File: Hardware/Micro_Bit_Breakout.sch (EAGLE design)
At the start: 9 parts, among them J1 M22LOCK, X1 EDGE-80PTH-RA

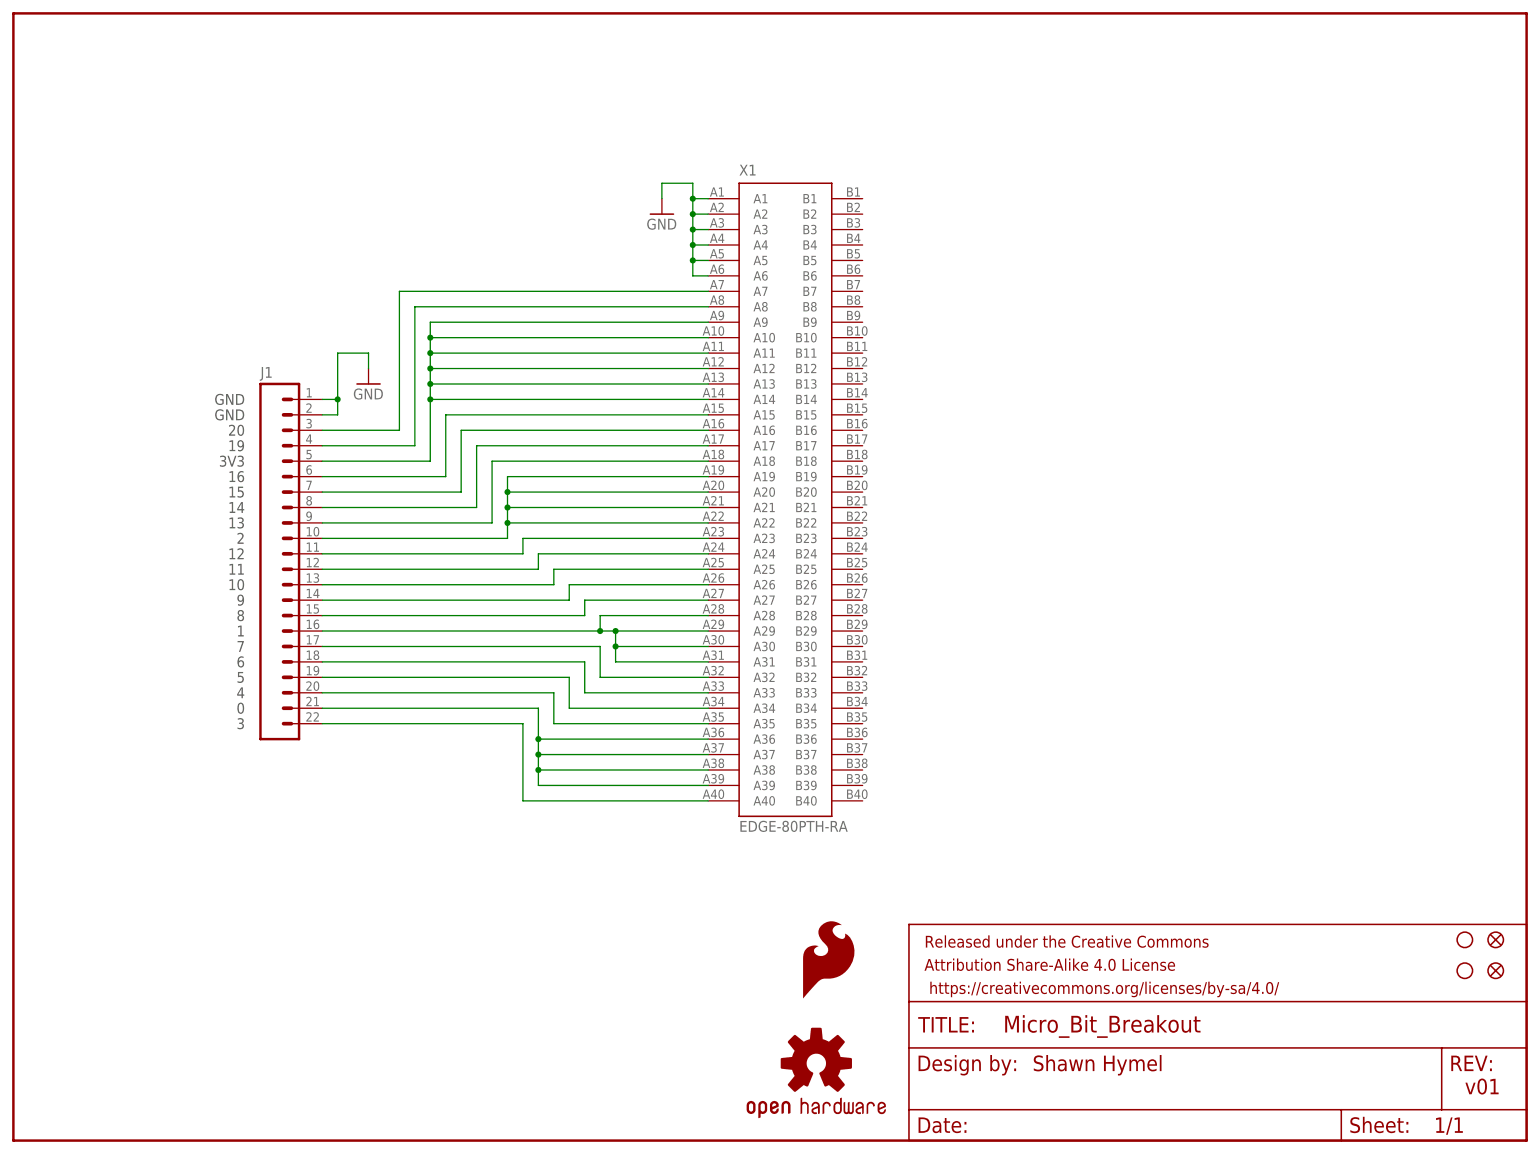
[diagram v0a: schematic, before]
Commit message: Moved brd outline down
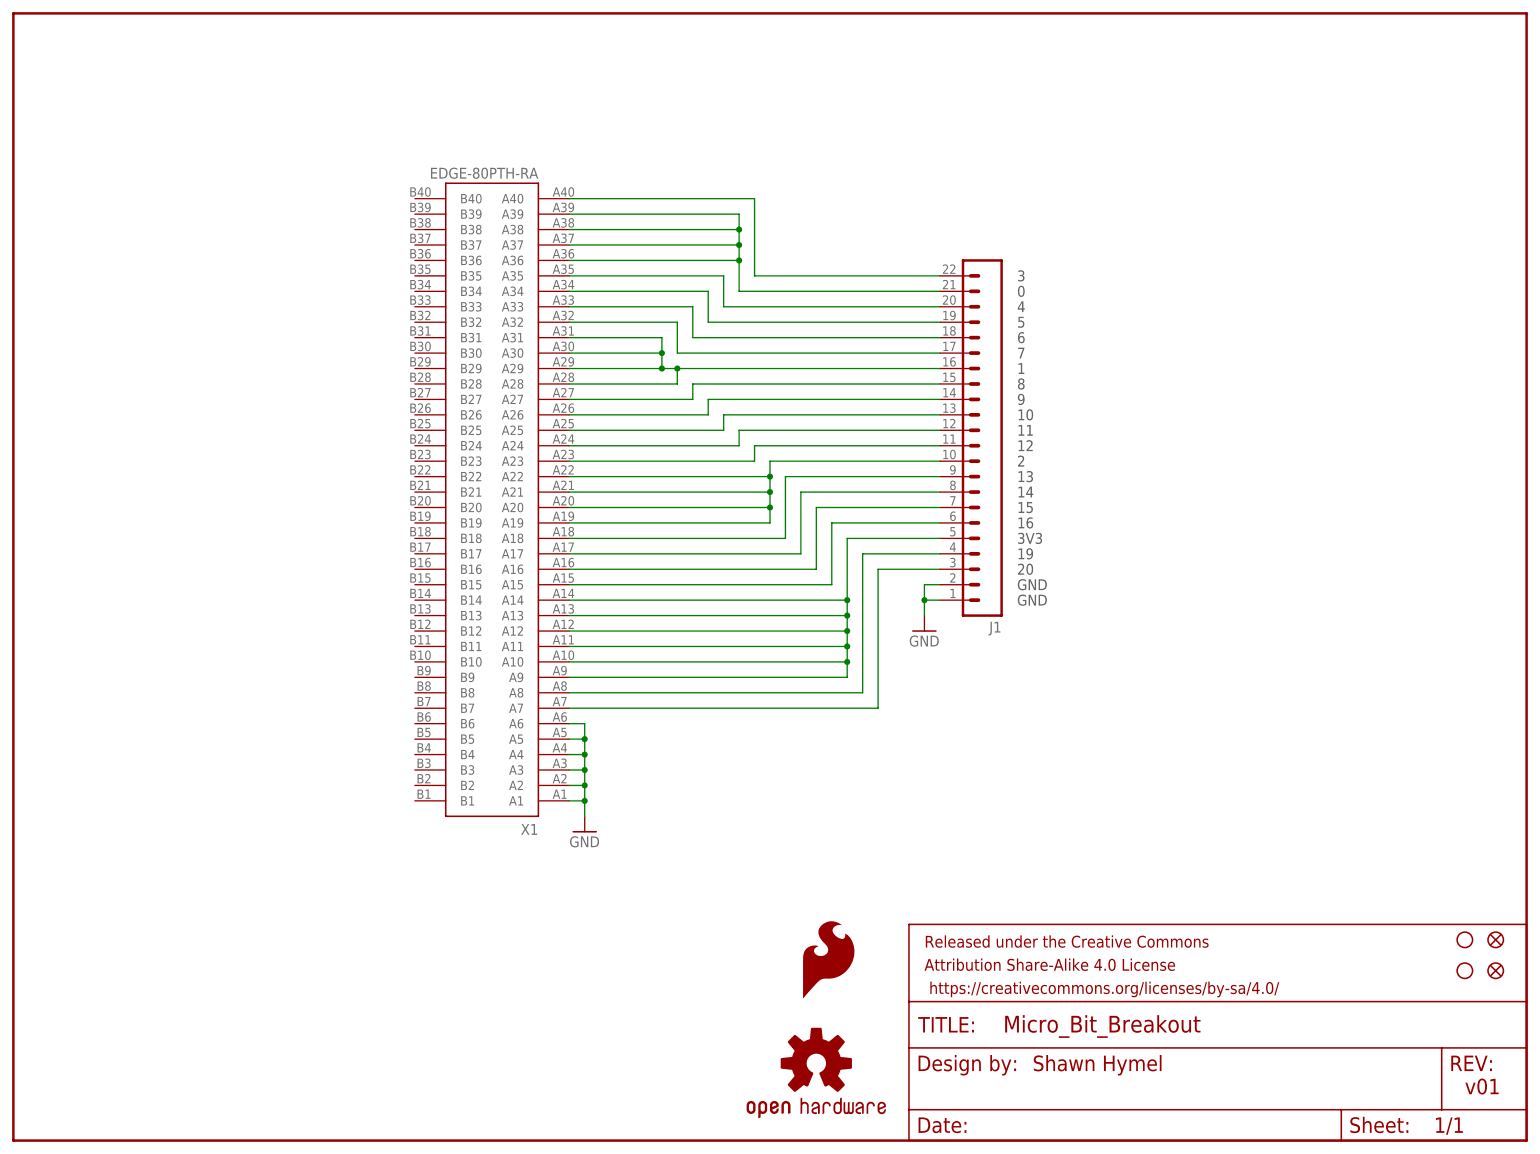
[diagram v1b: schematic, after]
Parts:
- J1: value M22LOCK -> M22PTH; device SparkFun-Connectors:M22LOCK -> local_lib:M22PTH
- X1: device SparkFun-Connectors:EDGE-80PTH-RA -> local_lib:EDGE-80PTH-RA
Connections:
- net N$10 renamed 12
- net N$11 renamed 11
- net N$12 renamed 10
- net N$13 renamed 9
- net N$14 renamed 8
- net N$15 renamed 1
- net N$17 renamed 7
- net N$18 renamed 6
- net N$19 renamed 5
- net N$2 renamed 16
- net N$20 renamed 4
- net N$21 renamed 0
- net N$22 renamed 3
- net N$3 renamed 20
- net N$4 renamed 19
- net N$5 renamed 3V3
- net N$6 renamed 15
- net N$7 renamed 14
- net N$8 renamed 13
- net N$9 renamed 2
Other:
- moved on the sheet: J1, X1

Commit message: Changed layout to have pin numbers in order. Added prettier silk.
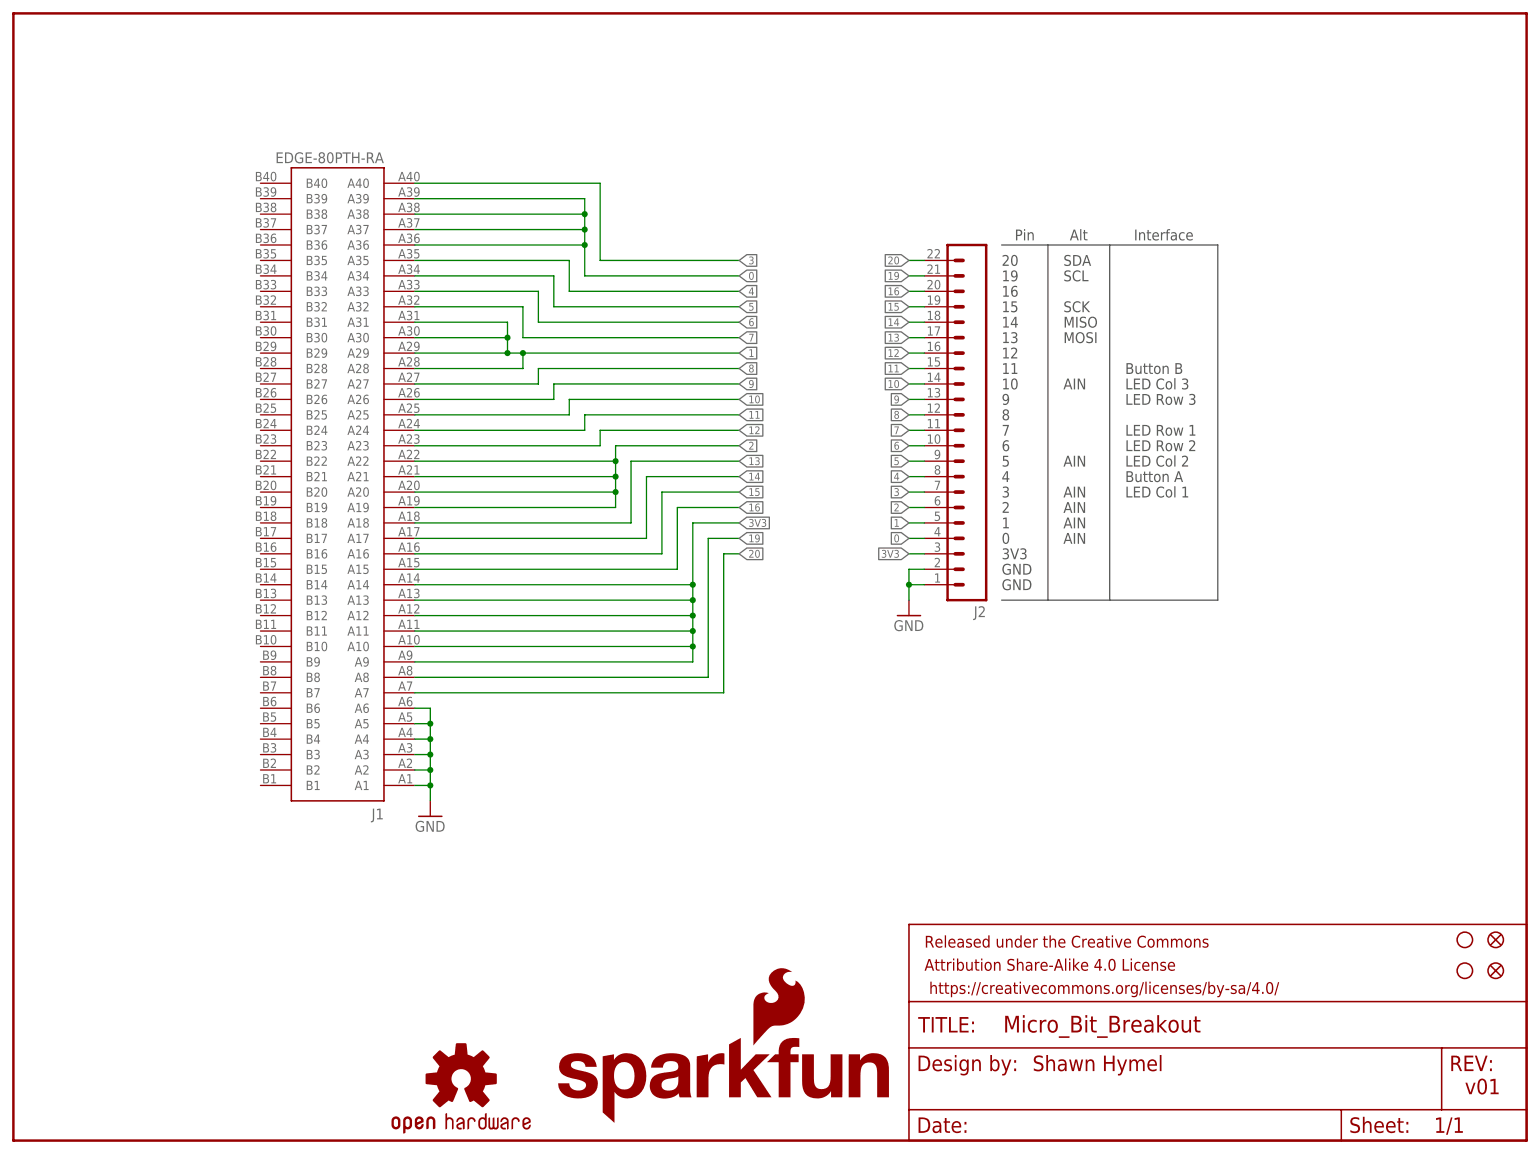
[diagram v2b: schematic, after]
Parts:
- removed LOGO1: SFE_LOGO_FLAME.1_INCH, SparkFun-Aesthetics:SFE_LOGO_FLAME.1_INCH
- removed X1: EDGE-80PTH-RA, local_lib:EDGE-80PTH-RA
- added J2: M22PTH, local_lib:M22PTH
- added LOGO2: SFE_LOGO_NAME_FLAME.1_INCH, SparkFun-Aesthetics:SFE_LOGO_NAME_FLAME.1_INCH
- J1: value M22PTH -> EDGE-80PTH-RA; device local_lib:M22PTH -> local_lib:EDGE-80PTH-RA
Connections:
- net 0: now also J1.A36, J1.A37, J1.A38, J1.A39, J2.4; no longer J1.21, X1.A36, X1.A37, X1.A38, X1.A39
- net 1: now also J1.A28, J1.A29, J1.A30, J1.A31, J2.5; no longer J1.16, X1.A28, X1.A29, X1.A30, X1.A31
- net 10: now also J1.A25, J2.14; no longer J1.13, X1.A25
- net 11: now also J1.A24, J2.15; no longer J1.12, X1.A24
- net 12: now also J1.A23, J2.16; no longer J1.11, X1.A23
- net 13: now also J1.A18, J2.17; no longer J1.9, X1.A18
- net 14: now also J1.A17, J2.18; no longer J1.8, X1.A17
- net 15: now also J1.A16, J2.19; no longer J1.7, X1.A16
- net 16: now also J1.A15, J2.20; no longer J1.6, X1.A15
- net 19: now also J1.A8, J2.21; no longer J1.4, X1.A8
- net 2: now also J1.A19, J1.A20, J1.A21, J1.A22, J2.6; no longer J1.10, X1.A19, X1.A20, X1.A21, X1.A22
- net 20: now also J1.A7, J2.22; no longer J1.3, X1.A7
- net 3: now also J1.A40, J2.7; no longer J1.22, X1.A40
- net 3V3: now also J1.A10, J1.A11, J1.A12, J1.A13, J1.A14, J1.A9, J2.3; no longer J1.5, X1.A10, X1.A11, X1.A12, X1.A13, X1.A14, X1.A9
- net 4: now also J1.A35, J2.8; no longer J1.20, X1.A35
- net 5: now also J1.A34, J2.9; no longer J1.19, X1.A34
- net 6: now also J1.A33, J2.10; no longer J1.18, X1.A33
- net 7: now also J1.A32, J2.11; no longer J1.17, X1.A32
- net 8: now also J1.A27, J2.12; no longer J1.15, X1.A27
- net 9: now also J1.A26, J2.13; no longer J1.14, X1.A26
- net GND: now also J1.A1, J1.A2, J1.A3, J1.A4, J1.A5, J1.A6, J2.1, J2.2; no longer J1.1, J1.2, X1.A1, X1.A2, X1.A3, X1.A4, X1.A5, X1.A6
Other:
- note added: "AIN"
- note added: "Alt"
- note added: "Button A"
- note added: "Button B"
- note added: "Interface"
- note added: "LED Col 1"
- note added: "LED Col 2"
- note added: "LED Col 3"
- note added: "LED Row 1"
- note added: "LED Row 2"
- note added: "LED Row 3"
- note added: "MISO"
- note added: "MOSI"
- note added: "Pin"
- note added: "SCK"
- note added: "SCL"
- note added: "SDA"

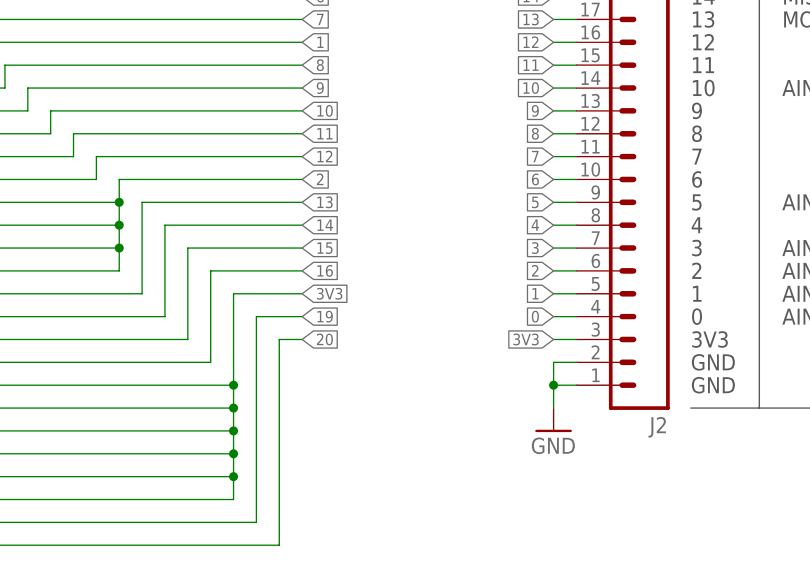
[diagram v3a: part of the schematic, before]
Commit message: Changed 3V3 net to 3.3V symbol
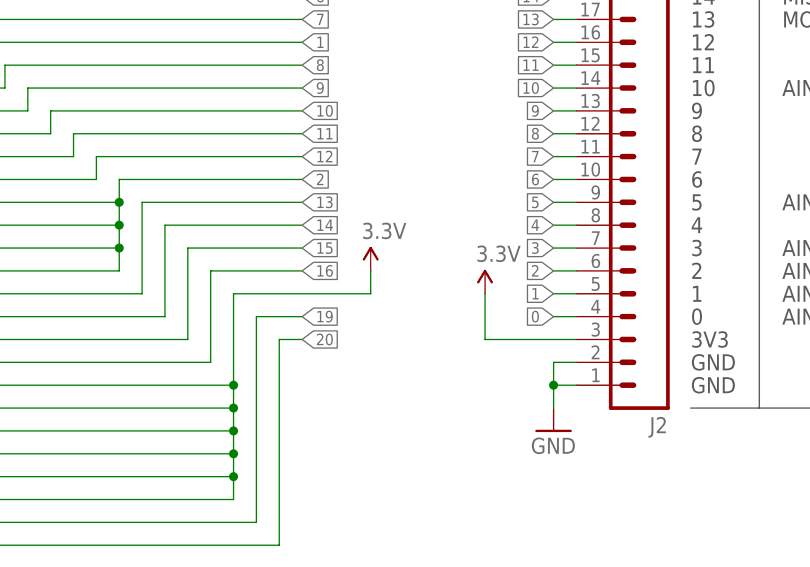
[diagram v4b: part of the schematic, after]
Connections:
- net 3V3 renamed 3.3V
